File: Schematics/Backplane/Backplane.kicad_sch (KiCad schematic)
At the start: 18 parts, among them J1 Edge Connector (SLOT 1), J2 Edge Connector (SLOT 2), J3 Edge Connector (SLOT 3), J4 Edge Connector (SLOT 4), J5 Edge Connector (SLOT 5), J6 Edge Connector (SLOT 6)

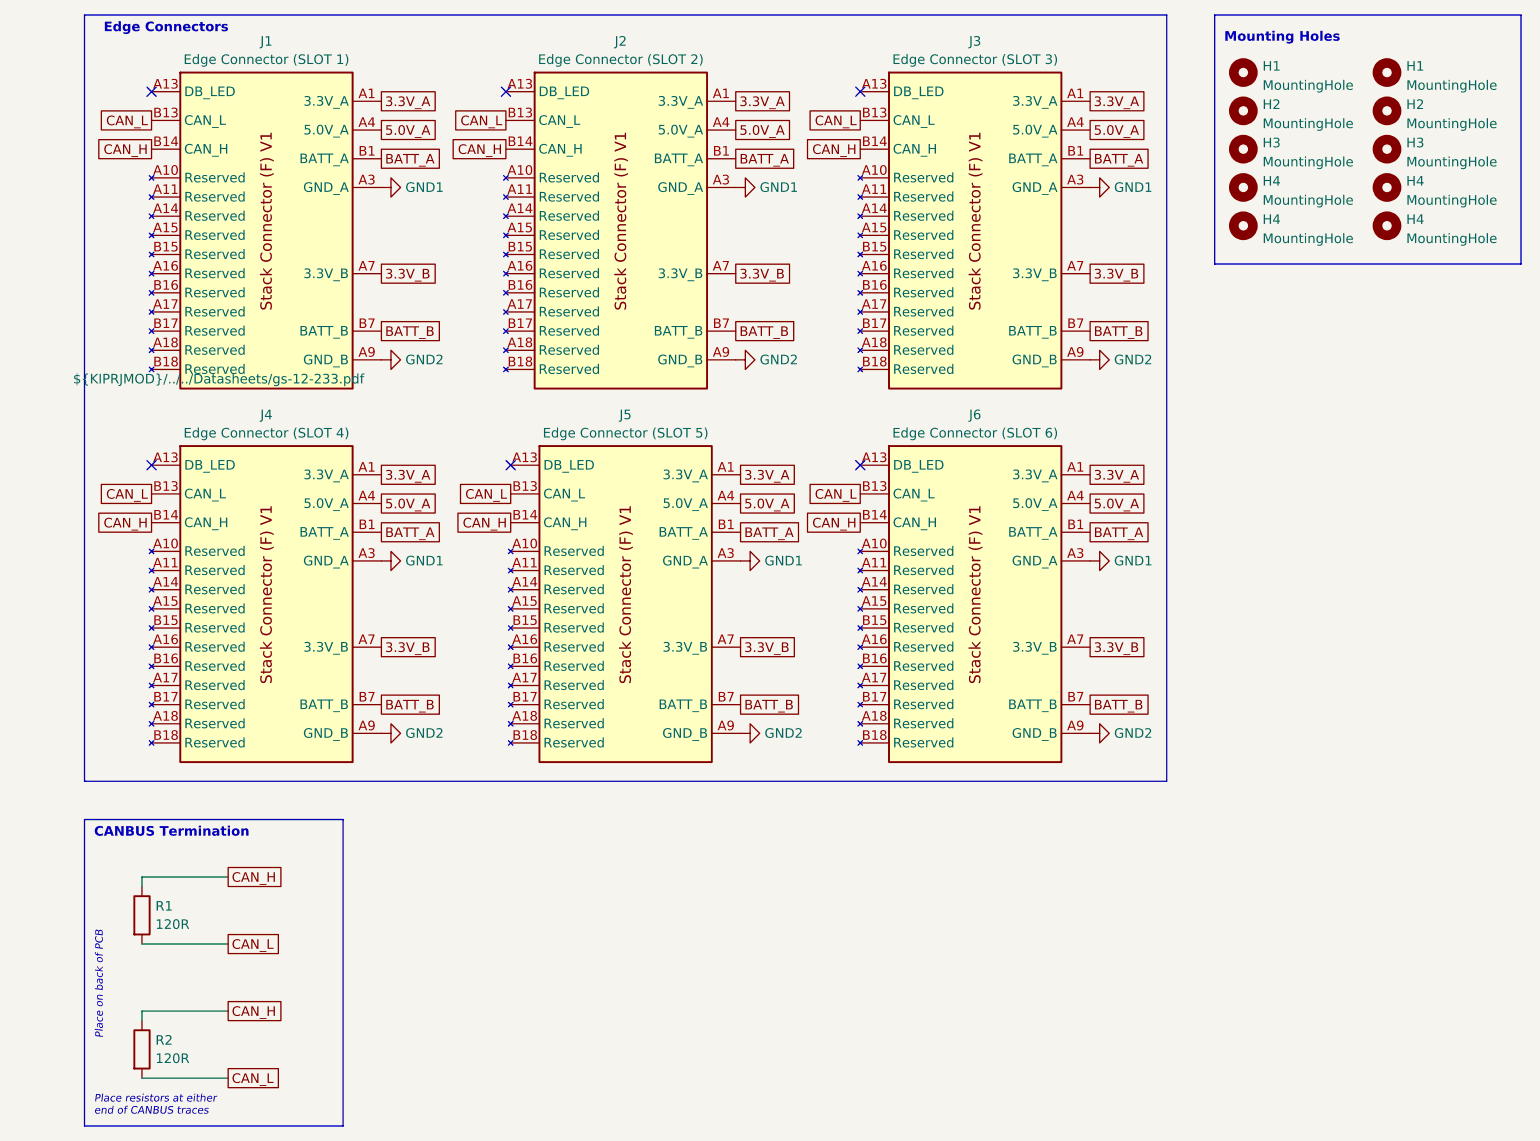
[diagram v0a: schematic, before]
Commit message: Current Updated Backplance
Did the wiring for the PCB. Not sure how to properly connect the edge connectors to the new connector (they don't want to connect)
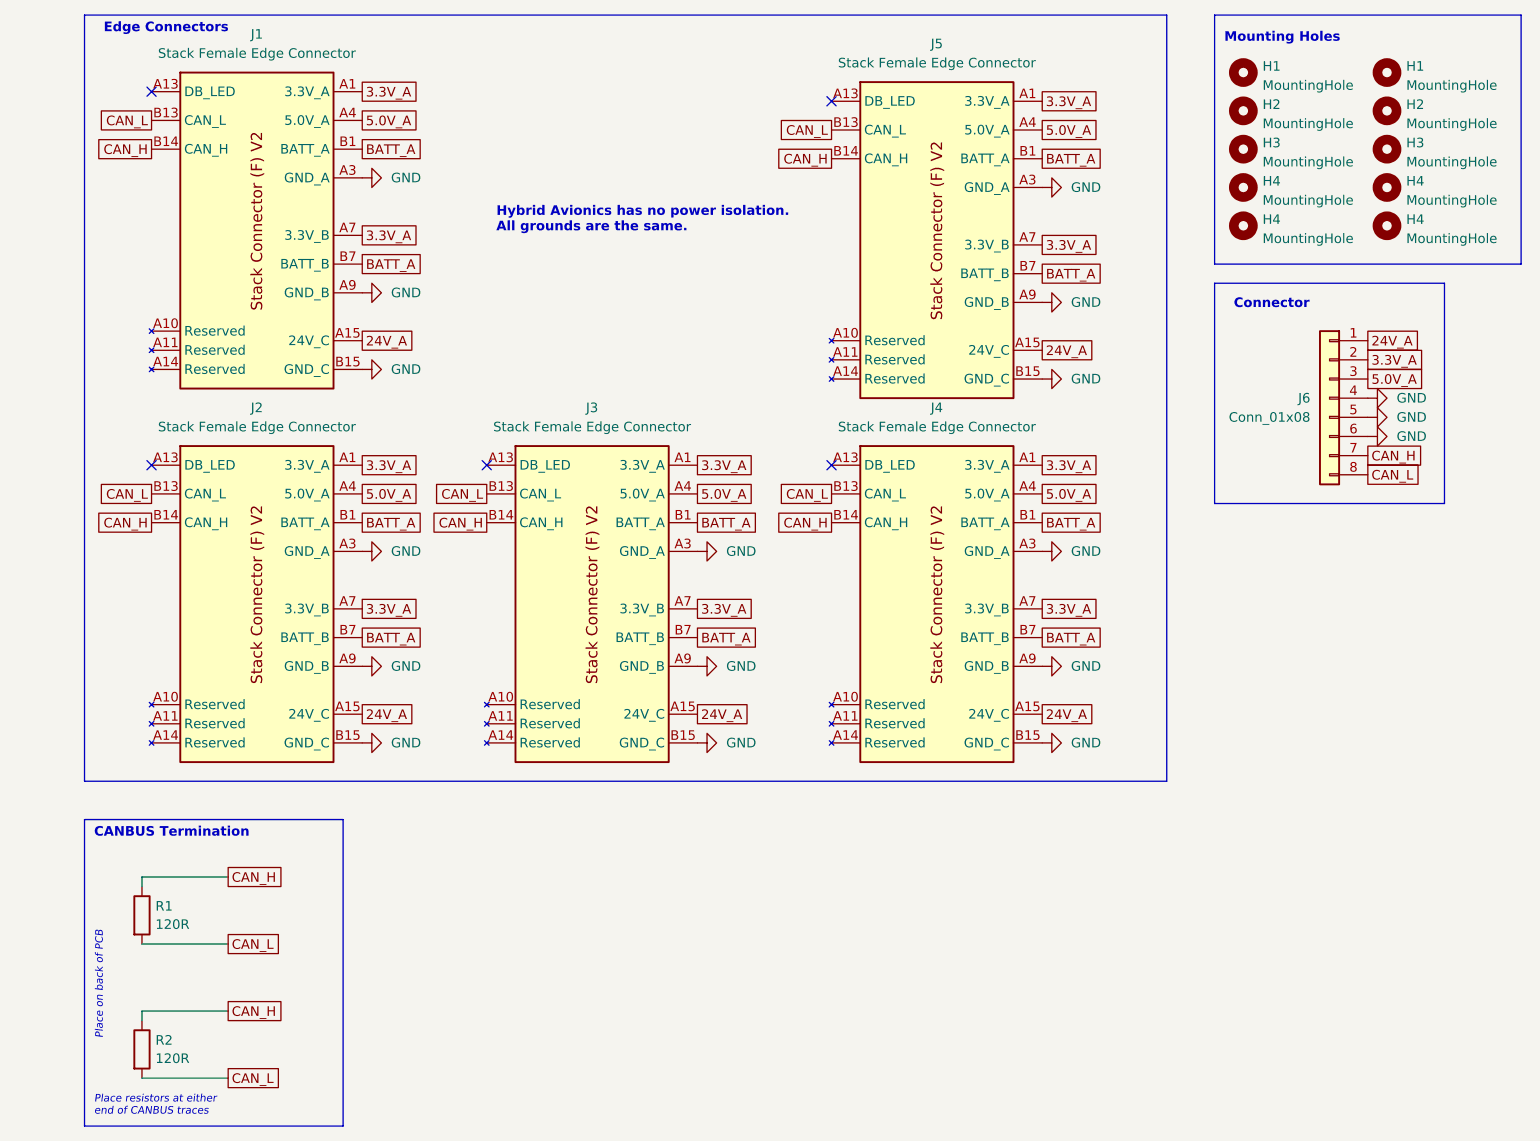
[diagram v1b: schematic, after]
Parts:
- removed J6: Edge Connector (SLOT 6), footprints:AMPHENOL_10018784-10210TLF, symbol EdgeConnector:Stack Female Edge Connector
- added J6: Conn_01x08, symbol Connector_Generic:Conn_01x08
- J1: value Edge Connector (SLOT 1) -> Stack Female Edge Connector; Digikey 609-2029-ND -> (none); Model 10018784-10210TLF -> (none)
- J2: value Edge Connector (SLOT 2) -> Stack Female Edge Connector; Digikey 609-2029-ND -> (none); Model 10018784-10210TLF -> (none)
- J3: value Edge Connector (SLOT 3) -> Stack Female Edge Connector; Digikey 609-2029-ND -> (none); Model 10018784-10210TLF -> (none)
- J4: value Edge Connector (SLOT 4) -> Stack Female Edge Connector; Digikey 609-2029-ND -> (none); Model 10018784-10210TLF -> (none)
- J5: value Edge Connector (SLOT 5) -> Stack Female Edge Connector; Digikey 609-2029-ND -> (none); Model 10018784-10210TLF -> (none)
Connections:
- net 3.3V_B is gone; now on net 3.3V_A: J1.A7 (3.3V_B), J1.A8 (3.3V_B), J2.A7 (3.3V_B), J2.A8 (3.3V_B), J3.A7 (3.3V_B), J3.A8 (3.3V_B), J4.A7 (3.3V_B), J4.A8 (3.3V_B), J5.A7 (3.3V_B), J5.A8 (3.3V_B)
- net BATT_B is gone; now on net BATT_A: J1.B7 (BATT_B), J1.B8 (BATT_B), J1.B9 (BATT_B), J2.B7 (BATT_B), J2.B8 (BATT_B), J2.B9 (BATT_B), J3.B7 (BATT_B), J3.B8 (BATT_B), J3.B9 (BATT_B), J4.B7 (BATT_B), J4.B8 (BATT_B), J4.B9 (BATT_B), J5.B7 (BATT_B), J5.B8 (BATT_B), J5.B9 (BATT_B)
- net GND1 is gone; now on net GND: J1.A3 (GND_A), J1.A6 (GND_A), J1.B4 (GND_A), J1.B5 (GND_A), J1.B6 (GND_A), J2.A3 (GND_A), J2.A6 (GND_A), J2.B4 (GND_A), J2.B5 (GND_A), J2.B6 (GND_A), J3.A3 (GND_A), J3.A6 (GND_A), J3.B4 (GND_A), J3.B5 (GND_A), J3.B6 (GND_A), J4.A3 (GND_A), J4.A6 (GND_A), J4.B4 (GND_A), J4.B5 (GND_A), J4.B6 (GND_A), J5.A3 (GND_A), J5.A6 (GND_A), J5.B4 (GND_A), J5.B5 (GND_A), J5.B6 (GND_A)
- net GND2 is gone; now on net GND: J1.A12 (GND_B), J1.A9 (GND_B), J1.B10 (GND_B), J1.B11 (GND_B), J1.B12 (GND_B), J2.A12 (GND_B), J2.A9 (GND_B), J2.B10 (GND_B), J2.B11 (GND_B), J2.B12 (GND_B), J3.A12 (GND_B), J3.A9 (GND_B), J3.B10 (GND_B), J3.B11 (GND_B), J3.B12 (GND_B), J4.A12 (GND_B), J4.A9 (GND_B), J4.B10 (GND_B), J4.B11 (GND_B), J4.B12 (GND_B), J5.A12 (GND_B), J5.A9 (GND_B), J5.B10 (GND_B), J5.B11 (GND_B), J5.B12 (GND_B)
- net 3.3V_A: now also J6.2 (Pin_2)
- net 5.0V_A: now also J6.3 (Pin_3)
- net CAN_H: now also J6.7 (Pin_7)
- net CAN_L: now also J6.8 (Pin_8)
- net 24V_A: now reaches J5.A15 (24V_C)
- net 24V_A: now also J1.A15 (24V_C), J1.A16 (24V_C), J1.A17 (24V_C), J1.A18 (24V_C), J2.A15 (24V_C), J2.A16 (24V_C), J2.A17 (24V_C), J2.A18 (24V_C), J3.A15 (24V_C), J3.A16 (24V_C), J3.A17 (24V_C), J3.A18 (24V_C), J4.A15 (24V_C), J4.A16 (24V_C), J4.A17 (24V_C), J4.A18 (24V_C), J5.A16 (24V_C), J5.A17 (24V_C), J5.A18 (24V_C), J6.1 (Pin_1)
- net GND: now reaches J5.B15 (GND_C)
- net GND: now also J1.B15 (GND_C), J1.B16 (GND_C), J1.B17 (GND_C), J1.B18 (GND_C), J2.B15 (GND_C), J2.B16 (GND_C), J2.B17 (GND_C), J2.B18 (GND_C), J3.B15 (GND_C), J3.B16 (GND_C), J3.B17 (GND_C), J3.B18 (GND_C), J4.B15 (GND_C), J4.B16 (GND_C), J4.B17 (GND_C), J4.B18 (GND_C), J5.B16 (GND_C), J5.B17 (GND_C), J5.B18 (GND_C), J6.4 (Pin_4), J6.5 (Pin_5), J6.6 (Pin_6)
- no-connect marks 6 -> 5
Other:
- note added: "Connector"
- note added: "Hybrid Avionics has no power isolation. All grounds are the same."
